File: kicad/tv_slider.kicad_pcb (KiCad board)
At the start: 2 copper layers, 119 x 93 mm, 71 parts, among them J1 MC 1,5/6-G-3.81, J2 MC 1,5/3-G-3.81, J3 MC 1,5/3-G-3.81, J4 MC 1,5/3-G-3.81, J5 MC 1,5/3-G-3.81, J6 MC 1,5/2-G-3.81, J7 MC 1,5/4-G-3.81, Q1 CSD19537Q3, Q2 BSS138, U1 LM5164DDA, U2 TPS26632RGE, U3 TPS82130, U4 TPS82130, U5 ESP32-C6-DEVKITC-1-N8, U6 DRV8452DDWR, U7 ISL3280ExHZ, U8 ISL3280ExHZ, U9 LS7184N-S

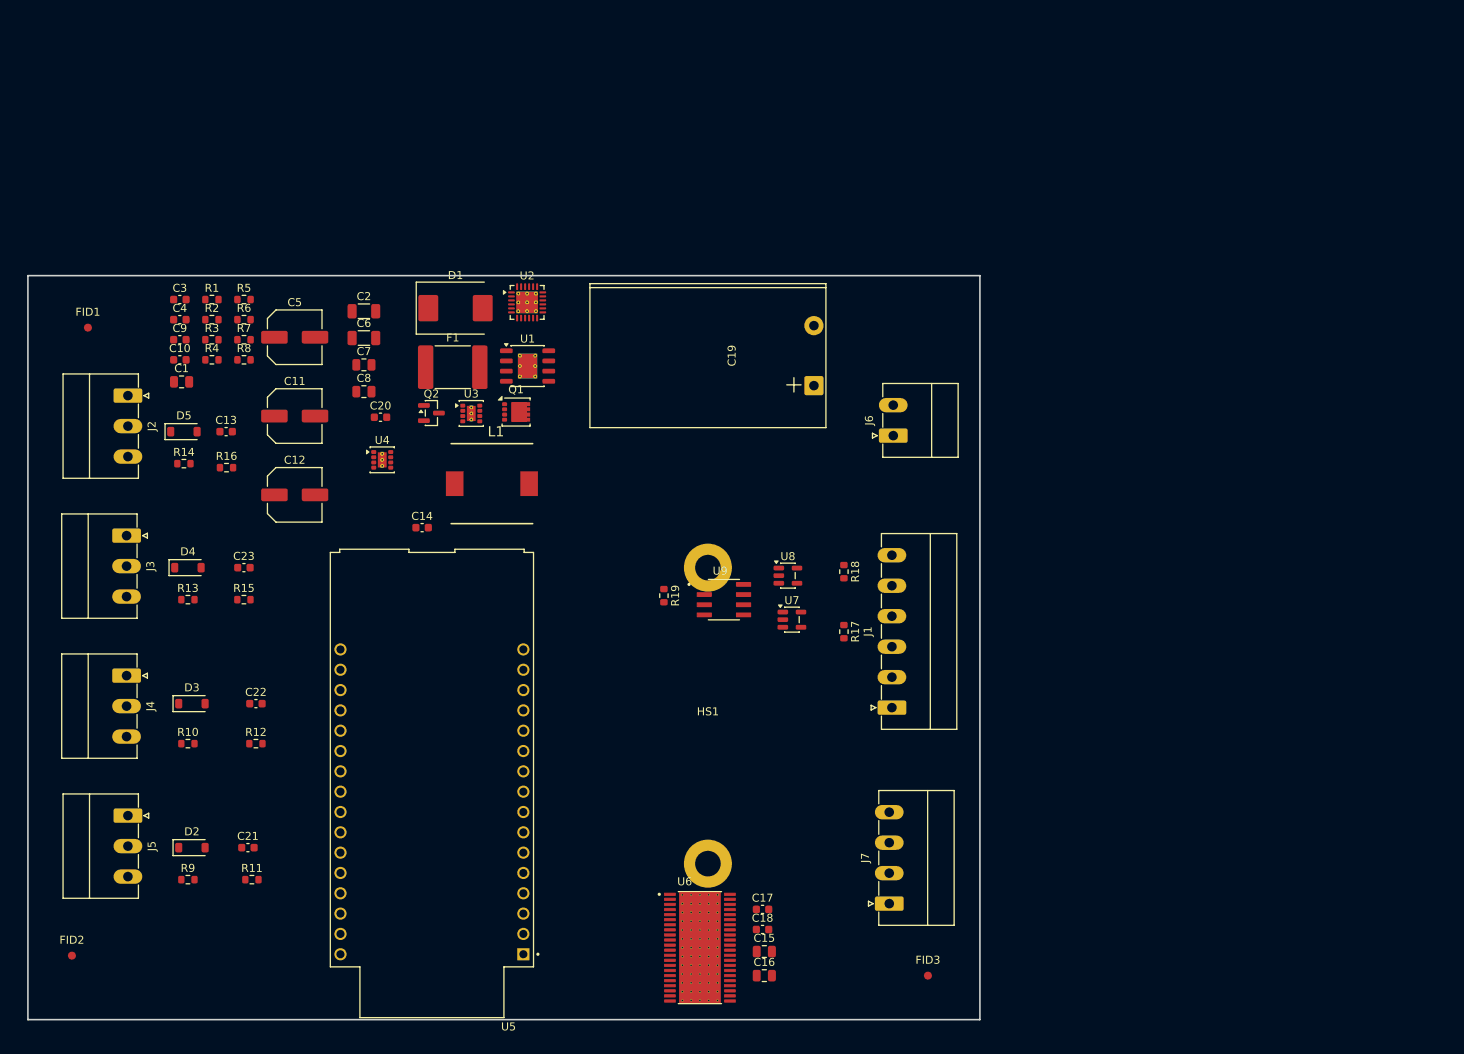
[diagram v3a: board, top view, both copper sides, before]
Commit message: Updated all schematic pages except the power supply. Did the initial component placement.
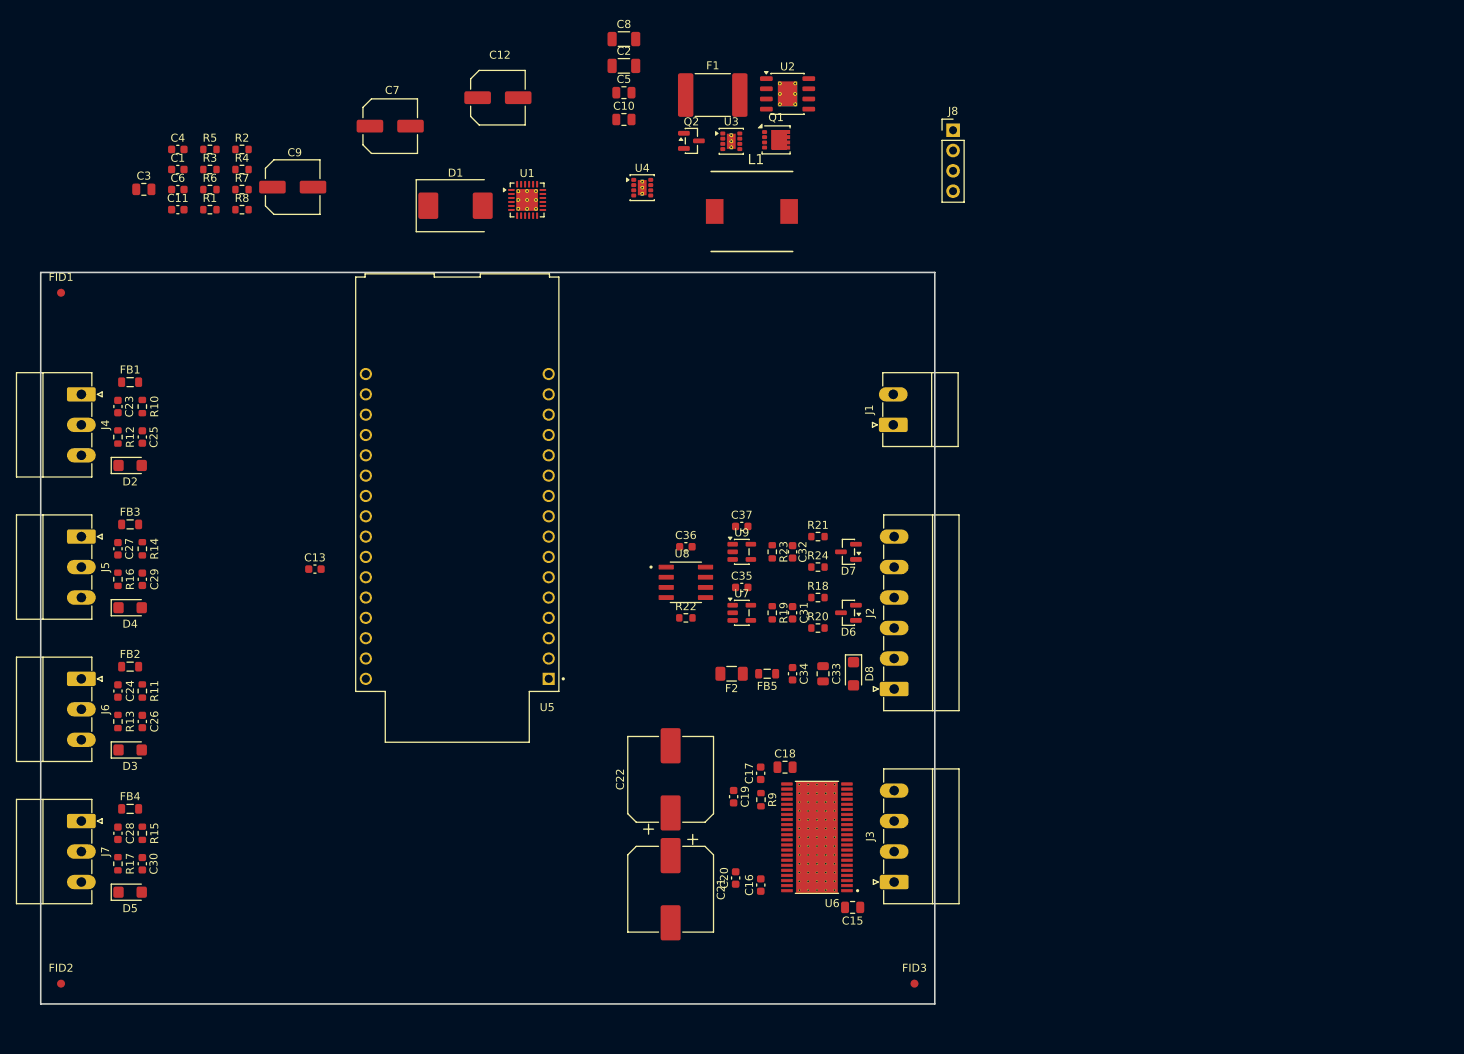
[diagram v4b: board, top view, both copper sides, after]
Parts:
- removed HS1: Heatsink_Pad, local_library:ATS-TI1OP-519-C1-R3
- added C17: 100n, Capacitor_SMD:C_0603_1608Metric, F.Cu at (128.1, 100.7)
- added C22: 150u, Capacitor_SMD:CP_Elec_10x12.5, F.Cu at (116.8, 101.5)
- added C23: 100n, Capacitor_SMD:C_0603_1608Metric, F.Cu at (47.8, 54.9)
- added C24: 100n, Capacitor_SMD:C_0603_1608Metric, F.Cu at (47.8, 90.4)
- added C27: 100n, Capacitor_SMD:C_0603_1608Metric, F.Cu at (47.8, 72.6)
- added C28: 100n, Capacitor_SMD:C_0603_1608Metric, F.Cu at (47.8, 108.2)
- added C31: 100p, Capacitor_SMD:C_0603_1608Metric, F.Cu at (132.1, 80.6)
- added C32: 100p, Capacitor_SMD:C_0603_1608Metric, F.Cu at (132.1, 73.0)
- added C33: 10u, Capacitor_SMD:C_0805_2012Metric, F.Cu at (135.9, 88.3)
- added C34: 100n, Capacitor_SMD:C_0603_1608Metric, F.Cu at (132.1, 88.3)
- added C35: 100n, Capacitor_SMD:C_0603_1608Metric, F.Cu at (125.7, 77.5)
- added C36: 100n, Capacitor_SMD:C_0603_1608Metric, F.Cu at (118.7, 72.4)
- added C37: 100n, Capacitor_SMD:C_0603_1608Metric, F.Cu at (125.7, 69.8)
- added D6: SM712_SOT23, Package_TO_SOT_SMD:SOT-23, F.Cu at (139.1, 80.6)
- added D7: SM712_SOT23, Package_TO_SOT_SMD:SOT-23, F.Cu at (139.1, 73.0)
- added D8: SMF6V0A, Diode_SMD:D_SMF, F.Cu at (139.7, 88.3)
- added F2: 0.2A, Fuse:Fuse_1206_3216Metric, F.Cu at (124.5, 88.3)
- added FB1: BLM21PG221SN1D, Inductor_SMD:L_0805_2012Metric, F.Cu at (49.3, 51.8)
- added FB2: BLM21PG221SN1D, Inductor_SMD:L_0805_2012Metric, F.Cu at (49.3, 87.4)
- added FB3: BLM21PG221SN1D, Inductor_SMD:L_0805_2012Metric, F.Cu at (49.3, 69.6)
- added FB4: BLM21PG221SN1D, Inductor_SMD:L_0805_2012Metric, F.Cu at (49.3, 105.2)
- added FB5: BLM21PG221SN1D, Inductor_SMD:L_0805_2012Metric, F.Cu at (128.9, 88.3)
- added J8: Conn_01x04, Connector_PinHeader_2.54mm:PinHeader_1x04_P2.54mm_Vertical, F.Cu at (152.1, 20.3)
- added R18: 10, Resistor_SMD:R_0603_1608Metric, F.Cu at (135.3, 78.7)
- added R20: 10, Resistor_SMD:R_0603_1608Metric, F.Cu at (135.3, 82.5)
- added R21: 10, Resistor_SMD:R_0603_1608Metric, F.Cu at (135.3, 71.1)
- added R24: 10, Resistor_SMD:R_0603_1608Metric, F.Cu at (135.3, 74.9)
- added R9: 100k, Resistor_SMD:R_0603_1608Metric, F.Cu at (128.1, 104.0)
- C21: renamed from C19; value 470u -> 150u; footprint local_library:CP_Radial_D18.0mm_P7.50mm_Horizontal -> Capacitor_SMD:CP_Elec_10x12.5
- D2, D3, D4, D5: value 3V6 -> SMF5V0A; footprint Diode_SMD:D_SOD-123 -> Diode_SMD:D_SMF
- R10: renamed from R11; value 10k -> 4.7k
- R11: renamed from R15; value 10k -> 4.7k
- R12: renamed from R9; value 100 -> 1k
- R13: value 100 -> 1k
- R14: renamed from R12; value 10k -> 4.7k
- R15: renamed from R16; value 10k -> 4.7k
- R16: renamed from R10; value 100 -> 1k
- R17: renamed from R14; value 100 -> 1k
- moved C21 65.4 mm to (116.8, 115.2), turned to -90 degrees
- moved C16 61.5 mm to (128.1, 114.7), turned to 90 degrees
- moved R10 60.7 mm to (50.8, 54.9), turned to 90 degrees
- moved D5 58.0 mm to (49.3, 115.6)
- moved R12 56.0 mm to (47.8, 58.7), turned to 90 degrees
- moved C12 55.8 mm to (95.2, 16.3)
- moved R17 50.7 mm to (47.8, 112.0), turned to 90 degrees
- moved D2 48.4 mm to (49.3, 62.2)
- moved Q1 47.0 mm to (130.0, 21.5)
- moved U2 47.0 mm to (131.5, 15.8)
- moved C8 47.0 mm to (111.0, 8.93)
- moved U3 47.0 mm to (124.4, 21.7)
- moved C10 47.0 mm to (111.0, 19.0)
- moved C2 47.0 mm to (111.0, 12.3)
- moved C5 47.0 mm to (111.0, 15.6)
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- renumbered C4 to C1, C8 to C10, C10 to C11, C14 to C16, C16 to C18, C17 to C19, C6 to C2, C18 to C20, C20 to C25, C22 to C26, C21 to C29, C1 to C3, C23 to C30, C3 to C4, C7 to C5, C9 to C6, C11 to C7, C2 to C8, C5 to C9, J6 to J1, J1 to J2, J7 to J3, J2 to J4, J3 to J5, J4 to J6, J5 to J7, R4 to R1, R17 to R19, R5 to R2, R19 to R22, R18 to R23, R2 to R3, R6 to R4, R1 to R5, R3 to R6, U2 to U1, U1 to U2, U9 to U8, U8 to U9
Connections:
- C10 pad 1: Net-(U3-EN) -> +12V
- C15 pad 1: Net-(U6-VCP) -> Vdrive
- C15 pad 2: GND -> Net-(U6-VCP)
- C5 pad 1: Net-(U3-EN) -> +12V
- D3 pad 1: /Location sensors/OUT_SLOW -> /Location sensors/IN_SLOW
- D4 pad 1: /Location sensors/IN_SLOW -> /Location sensors/OUT_SLOW
- F1 pad 2: Net-(U3-EN) -> +12V
- J2 pad 2: +5V -> /Shaft encoder/+5Vout
- J4 pad 1: +12V -> /Location sensors/+12V_SENSOR_OUT_STOP
- J5 pad 1: +12V -> /Location sensors/+12V_SENSOR_OUT_SLOW
- J6 pad 1: +12V -> /Location sensors/+12V_SENSOR_IN_SLOW
- J7 pad 1: +12V -> /Location sensors/+12V_SENSOR_IN_STOP
- R19 pad 1: /Shaft encoder/A+ -> Net-(U7-A)
- R19 pad 2: /Shaft encoder/A- -> Net-(U7-B)
- R23 pad 1: /Shaft encoder/B+ -> Net-(U9-A)
- R23 pad 2: /Shaft encoder/B- -> Net-(U9-B)
- U3 pad 1: Net-(U3-EN) -> +12V
- U3 pad 2: Net-(U3-EN) -> +12V
- U4 pad 1: Net-(U3-EN) -> +12V
- U4 pad 2: Net-(U3-EN) -> +12V
- U5 pad J1_5: unconnected-(U5-GPIO6-PadJ1_5) -> Net-(J8-Pin_1)
- U5 pad J1_7: unconnected-(U5-GPIO0-PadJ1_7) -> /MCU/~{HOME}
- U5 pad J1_8: unconnected-(U5-GPIO1-PadJ1_8) -> Net-(J8-Pin_2)
- U5 pad J1_9: unconnected-(U5-GPIO8-PadJ1_9) -> Net-(J8-Pin_3)
- U6 pad 27: unconnected-(U6-~{HOME}-Pad27) -> /MCU/~{HOME}
- U6 pad 33: unconnected-(U6-VREF-Pad33) -> GND
- U7 pad 4: /Shaft encoder/A- -> Net-(U7-B)
- U7 pad 5: /Shaft encoder/A+ -> Net-(U7-A)
- U9 pad 4: /Shaft encoder/B- -> Net-(U9-B)
- U9 pad 5: /Shaft encoder/B+ -> Net-(U9-A)
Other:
- board size 119 x 93 mm -> 111.8 x 91.4 mm

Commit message: Finished the schematic and started the PCB.
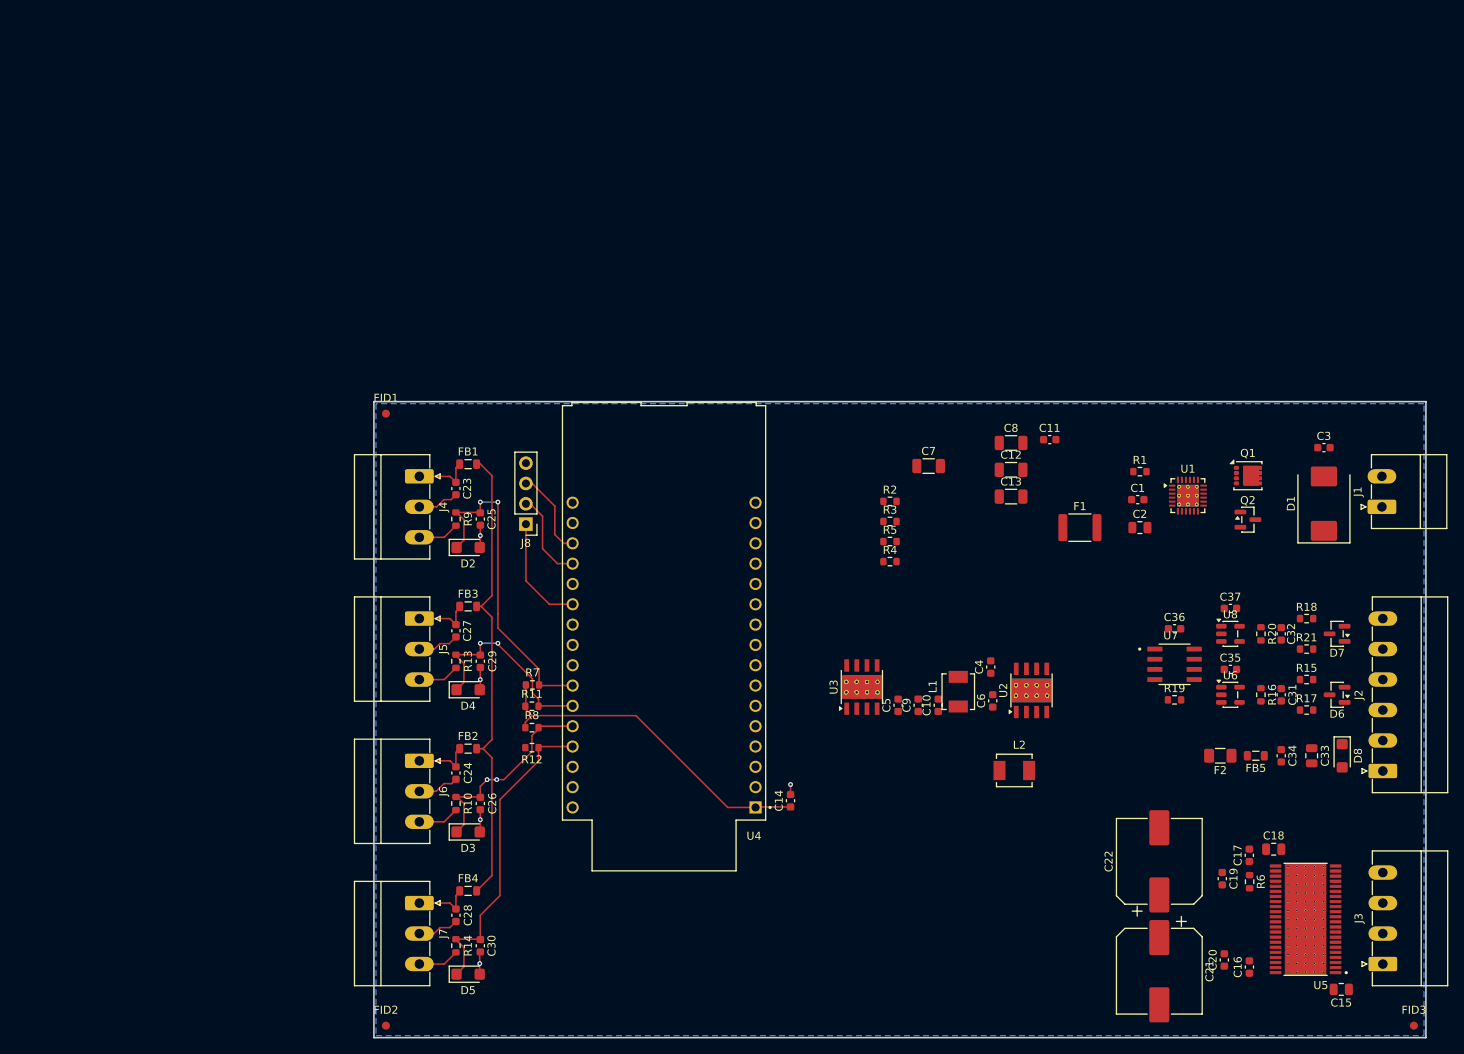
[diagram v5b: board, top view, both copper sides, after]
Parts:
- removed the C2 at (111.0, 12.3)
- removed the R3 at (59.2, 25.2)
- removed the R5 at (59.2, 22.7)
- removed the R6 at (59.2, 27.7)
- removed the U4 at (113.3, 27.5)
- added C13: 22u, Capacitor_SMD:C_1206_3216Metric, F.Cu at (159.4, 66.1)
- added C5: 220n, Capacitor_SMD:C_0603_1608Metric, F.Cu at (145.3, 92.2)
- added L2: 10u, local_library:IND_SRP4020TA-100M, F.Cu at (159.8, 100.4)
- C10: value 10u -> 220n; footprint Capacitor_SMD:C_0805_2012Metric -> Capacitor_SMD:C_0603_1608Metric
- C11, C6: value 3.3n -> 1u
- C12, C7: footprint Capacitor_SMD:C_Elec_6.3x5.8 -> Capacitor_SMD:C_1206_3216Metric
- C3: footprint Capacitor_SMD:C_0805_2012Metric -> Capacitor_SMD:C_0603_1608Metric
- C4: value 2.2n -> 100n
- C8: value 2.2u -> 22u
- C9: value 47u -> 100n; footprint Capacitor_SMD:C_Elec_6.3x5.8 -> Capacitor_SMD:C_0603_1608Metric
- D1: value 1.5SMCxxCA -> 1.5SMC33CA
- F1: value 1.1A -> 300mA; footprint local_library:Fuse_2920_7451Metric -> Fuse:Fuse_1812_4532Metric
- L1: value 68u -> 10u; footprint local_library:INDPM102100X400N -> local_library:IND_SRP4020TA-100M
- R2: value 526k -> 100k
- R3: renamed from R4; value 100k -> 24.9k
- R5: renamed from R7; value 316k -> 43.2k
- U2: value LM5164DDA -> LMR33610ADDAR; footprint Package_SO:HSOP-8-1EP_3.9x4.9mm_P1.27mm_EP2.41x3.1mm_ThermalVias -> local_library:Texas_HSOP-8-1EP_3.9x4.9mm_P1.27mm_ThermalVias
- U3: value TPS82130 -> LMR33610ADDAR; footprint local_library:Texas_SIL0008D_MicroSiP-8-1EP_2.8x3mm_P0.65mm_EP1.1x1.9mm_ThermalVias -> local_library:Texas_HSOP-8-1EP_3.9x4.9mm_P1.27mm_ThermalVias
- moved C3 151.0 mm to (198.5, 60.0)
- moved C1 126.9 mm to (175.2, 66.5)
- moved R1 120.8 mm to (175.5, 63.0)
- moved C4 120.5 mm to (156.9, 87.4), turned to 90 degrees
- moved C6 120.3 mm to (157.1, 91.7), turned to 90 degrees
- moved D1 114.8 mm to (198.5, 67.0), turned to 90 degrees
- moved C11 112.7 mm to (164.2, 59.0)
- moved C9 101.5 mm to (147.8, 92.2), turned to 90 degrees
- moved R3 92.2 mm to (144.3, 69.2)
- moved R4 92.2 mm to (144.3, 74.2)
- moved R5 92.2 mm to (144.3, 71.7)
- moved R2 92.2 mm to (144.3, 66.7)
- moved U1 90.5 mm to (181.5, 66.0)
- moved C2 84.4 mm to (175.5, 70.0)
- moved Q2 84.1 mm to (189.0, 69.0)
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- renumbered C13 to C14, C5 to C2, R13 to R10, R14 to R11, R15 to R12, R16 to R13, R17 to R14, R18 to R15, R19 to R16, R20 to R17, R21 to R18, R22 to R19, R23 to R20, R24 to R21, R8 to R4, R9 to R6, R10 to R7, R11 to R8, R12 to R9, U5 to U4, U6 to U5, U7 to U6, U8 to U7, U9 to U8
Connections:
- net /Location sensors/+12V_SENSOR_IN_SLOW renamed /Location sensors/+5V_SENSOR_IN_SLOW
- net /Location sensors/+12V_SENSOR_IN_STOP renamed /Location sensors/+5V_SENSOR_IN_STOP
- net /Location sensors/+12V_SENSOR_OUT_SLOW renamed /Location sensors/+5V_SENSOR_OUT_SLOW
- net /Location sensors/+12V_SENSOR_OUT_STOP renamed /Location sensors/+5V_SENSOR_OUT_STOP
- C10 pad 1: +12V -> Net-(U2-EN)
- C11 pad 1: Net-(U4-SS/TR) -> Net-(U3-VCC)
- C2 pad 1: +12V -> Vdrive
- C6 pad 1: Net-(U3-SS/TR) -> Net-(U2-VCC)
- C8 pad 1: Vdrive -> +5V
- C9 pad 1: Net-(C9-Pad1) -> Net-(U3-BOOT)
- C9 pad 2: GND -> Net-(U3-SW)
- F1 pad 1: Net-(C9-Pad1) -> Net-(U2-EN)
- F1 pad 2: +12V -> Vdrive
- FB1 pad 2: +12V -> +5V
- FB2 pad 2: +12V -> +5V
- FB3 pad 2: +12V -> +5V
- FB4 pad 2: +12V -> +5V
- L1 pad 2: Net-(C9-Pad1) -> +5V
- Q1 pad 1: Net-(Q1-S-Pad1) -> /Power supply/Vin
- Q1 pad 2: Net-(Q1-S-Pad1) -> /Power supply/Vin
- Q1 pad 3: Net-(Q1-S-Pad1) -> /Power supply/Vin
- Q1 pad 5: /Power supply/Vin -> Net-(Q1-D)
- Q2 pad 2: Net-(Q1-G) -> /Power supply/Vin
- Q2 pad 3: /Power supply/Vin -> Net-(Q1-G)
- R2 pad 2: Net-(U3-FB) -> Net-(U2-FB)
- R3 pad 1: Net-(U3-FB) -> Net-(U2-FB)
- R4 pad 1: Net-(U4-FB) -> +3.3V
- R4 pad 2: GND -> Net-(U3-FB)
- R5 pad 1: +3.3V -> Net-(U3-FB)
- R5 pad 2: Net-(U4-FB) -> GND
- U1 pad 1: Net-(Q1-S-Pad1) -> Net-(Q1-D)
- U1 pad 2: Net-(Q1-S-Pad1) -> Net-(Q1-D)
- U2 pad 2: Vdrive -> Net-(U2-EN)
- U2 pad 3: Vdrive -> Net-(U2-EN)
- U2 pad 4: Net-(U2-RON) -> unconnected-(U2-PG-Pad4)
- U2 pad 6: unconnected-(U2-PGOOD-Pad6) -> Net-(U2-VCC)
- U3 pad 1: +12V -> GND
- U3 pad 2: +12V -> Net-(U2-EN)
- U3 pad 3: GND -> Net-(U2-EN)
- U3 pad 4: +5V -> unconnected-(U3-PG-Pad4)
- U3 pad 5: +5V -> Net-(U3-FB)
- U3 pad 6: Net-(U3-FB) -> Net-(U3-VCC)
- U3 pad 7: unconnected-(U3-PG-Pad7) -> Net-(U3-BOOT)
- U3 pad 8: Net-(U3-SS/TR) -> Net-(U3-SW)
- U4 pad J1_10: /Location sensors/OUT_STOP -> unconnected-(U4-GPIO10-PadJ1_10)
- U4 pad J1_11: /Location sensors/OUT_SLOW -> unconnected-(U4-GPIO11-PadJ1_11)
- U4 pad J1_12: /Location sensors/IN_SLOW -> unconnected-(U4-GPIO2-PadJ1_12)
- U4 pad J1_13: /Location sensors/IN_STOP -> unconnected-(U4-GPIO3-PadJ1_13)
- U4 pad J1_3: /MCU/COUNT -> unconnected-(U4-GPIO4-PadJ1_3)
- U4 pad J1_4: /MCU/UP/~{DOWN} -> unconnected-(U4-GPIO5-PadJ1_4)
- U4 pad J1_5: Net-(J8-Pin_1) -> unconnected-(U4-GPIO6-PadJ1_5)
- U4 pad J1_6: /MCU/~{FAULT} -> unconnected-(U4-GPIO7-PadJ1_6)
- U4 pad J1_7: /MCU/~{HOME} -> unconnected-(U4-GPIO0-PadJ1_7)
- U4 pad J1_8: Net-(J8-Pin_2) -> unconnected-(U4-GPIO1-PadJ1_8)
- U4 pad J1_9: Net-(J8-Pin_3) -> unconnected-(U4-GPIO8-PadJ1_9)
- U4 pad J3_10: /MCU/DIR -> unconnected-(U4-GPIO18-PadJ3_10)
- U4 pad J3_11: /MCU/STEP -> Net-(J8-Pin_1)
- U4 pad J3_13: /MCU/~{SLEEP} -> Net-(J8-Pin_2)
- U4 pad J3_14: unconnected-(U5-GPIO12-PadJ3_14) -> Net-(J8-Pin_3)
- U4 pad J3_4: /MCU/~{CS} -> /Location sensors/IN_STOP
- U4 pad J3_5: /MCU/SCLK -> /Location sensors/IN_SLOW
- U4 pad J3_6: /MCU/MOSI -> /Location sensors/OUT_SLOW
- U4 pad J3_7: /MCU/MISO -> /Location sensors/OUT_STOP
- U4 pad J3_9: /MCU/ENABLE -> unconnected-(U4-GPIO19-PadJ3_9)
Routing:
- net +5V: track 0.00 -> 58.6 mm
- net +3V3: track 0.00 -> 43.2 mm
- net /Location sensors/OUT_STOP: track 0.00 -> 41.5 mm, vias 0 -> 2
- net /Location sensors/IN_STOP: track 0.00 -> 39.8 mm
- net GND: track 0.00 -> 34.4 mm, vias 0 -> 5
- net /Location sensors/OUT_SLOW: track 0.00 -> 26.2 mm, vias 0 -> 2
- net /Location sensors/IN_SLOW: track 0.00 -> 25.9 mm, vias 0 -> 2
- net Net-(J8-Pin_1): track 0.00 -> 14.1 mm
- net Net-(J8-Pin_2): track 0.00 -> 11.3 mm
- net Net-(J8-Pin_3): track 0.00 -> 11.0 mm
- net /Location sensors/+5V_SENSOR_IN_SLOW: track 0.00 -> 7.35 mm
- net /Location sensors/+5V_SENSOR_OUT_STOP: track 0.00 -> 7.35 mm
- net /Location sensors/+5V_SENSOR_IN_STOP: track 0.00 -> 7.35 mm
- net /Location sensors/+5V_SENSOR_OUT_SLOW: track 0.00 -> 7.35 mm
- net /Location sensors/SENSOR_OUT_STOP: track 0.00 -> 5.18 mm
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- added copper zone on B.Cu, net GND
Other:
- board size 111.8 x 91.4 mm -> 131.5 x 79.5 mm
